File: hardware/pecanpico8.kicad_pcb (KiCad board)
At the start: 4 copper layers, 29.8 x 33.7 mm, 153 parts, among them IC1 SPV1040, IC2 TPS62260, IC3 ADP322ACPZ-115-R7, IC4 Si4464, IC5 STM32F745IGKx, IC6 EVA-7M, IC7 PAC1720, IC8 BME280, P1 CONN_01X25, P2 CONN_01X11, P3 USB_OTG, P4 SMA Edge, P5 CONN_01X02, Q1 FDN306P, X1 KT2016K26000BCW18ZAS

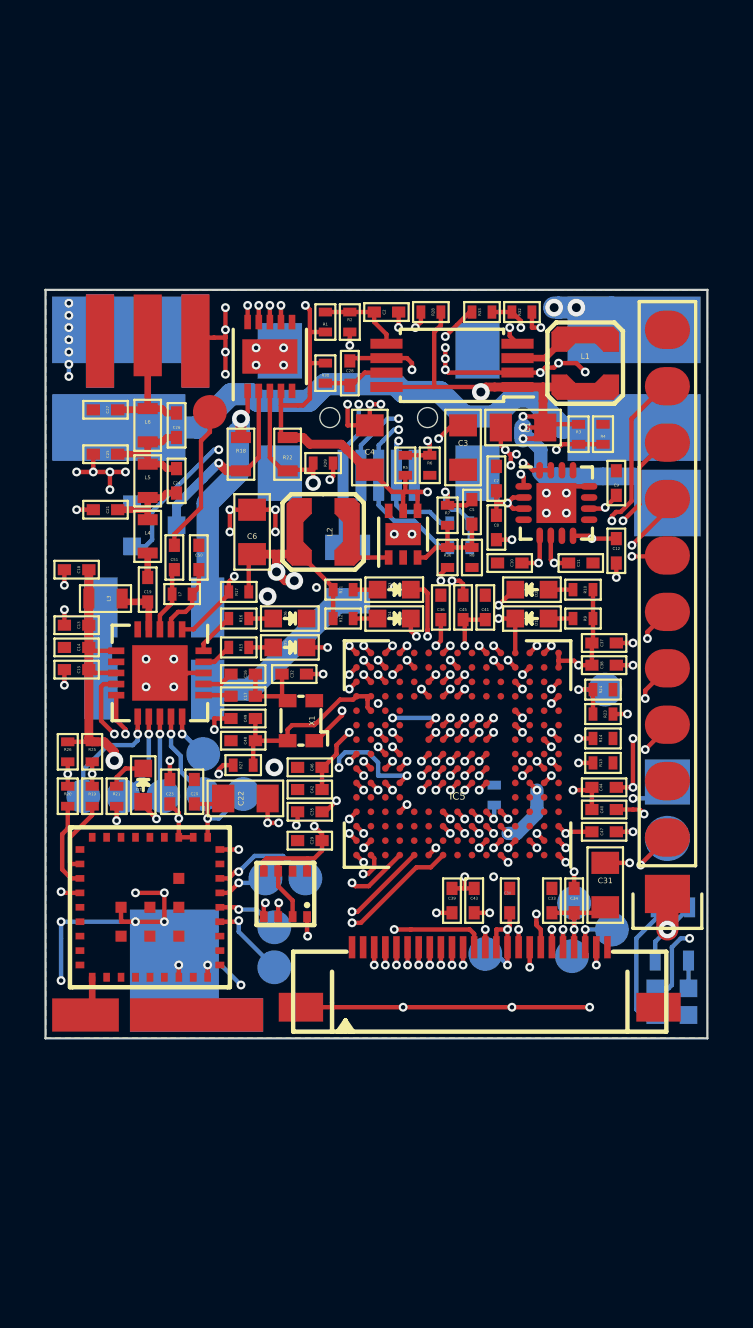
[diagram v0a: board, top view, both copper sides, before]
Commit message: Started developement of rev 8b Changed USB Connector: Mini => Micro Connected CAM_EN to STM32 Added battery jumper switch at programming header Added solar input at programmer header Removed LED outputs at programmer header Removed Testpads at BOOT0 Moved parts around
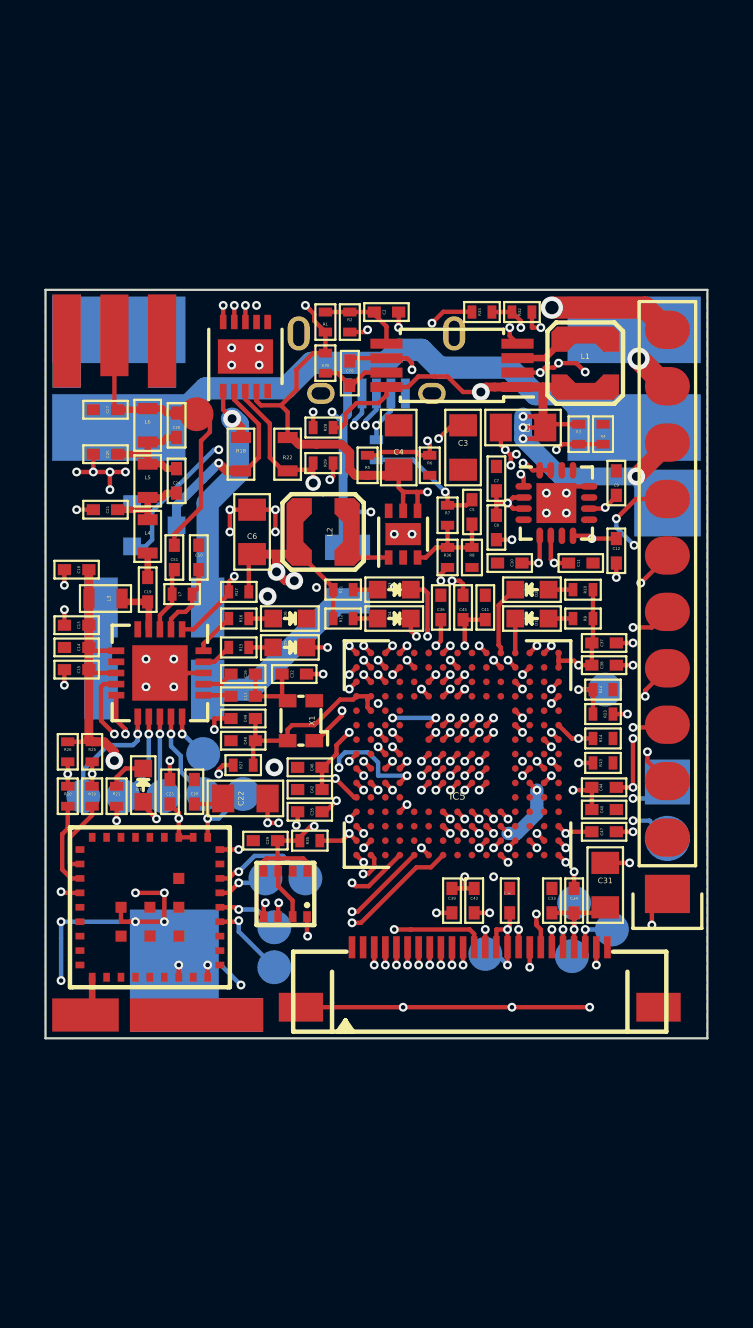
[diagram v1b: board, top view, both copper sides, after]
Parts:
- removed D10: red, stm32f7:LED_0603
- removed D11: yellow, stm32f7:LED_0603
- removed R34: 1k5, stm32f7:R_0603
- removed R37: 330R, stm32f7:R_0603
- removed W1: TEST, stm32f7:R_0402
- P3: footprint Connect:USB_Mini-B -> stm32f7:USB_Micro-B
- R35: moved to F.Cu
- moved R35 14.8 mm to (59.0, 115.7), turned to 0 degrees
- moved R28 7.11 mm to (59.6, 97.1)
- moved R31 5.00 mm to (62.0, 98.1), turned to 90 degrees
- moved C29 2.00 mm to (57.0, 115.7)
- moved P3 1.80 mm to (62.0, 94.0), turned to 0 degrees
- moved R5 1.70 mm to (61.6, 98.8)
- moved P4 1.50 mm to (50.2, 91.1)
- moved C4 1.30 mm to (63.0, 98.0)
- moved IC7 1.10 mm to (56.1, 93.9)
- moved W25 0.61 mm to (53.9, 96.5)
- moved R30 0.45 mm to (59.7, 94.2)
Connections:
- F1 pad 2: Net-(F1-Pad2) -> /USB_VUSB
- IC5 pad E15: Net-(IC5-PadE15) -> /USB_VUSB
- IC5 pad K1: Net-(IC5-PadK1) -> /CAM_EN
- P2 pad 1: +1V8 -> /SWD_SWCLK
- P2 pad 10: /IO_RXD -> /BATT_CONN
- P2 pad 11: GND -> +BATT
- P2 pad 2: /SWD_SWCLK -> GND
- P2 pad 3: GND -> /SWD_SWDIO
- P2 pad 4: /SWD_SWDIO -> /SWD_NRST
- P2 pad 5: /SWD_NRST -> /SWD_SWO
- P2 pad 6: /SWD_SWO -> /IO_TXD
- P2 pad 7: /IO_LED1 -> /IO_RXD
- P2 pad 8: /IO_LED2 -> GND
- P2 pad 9: /IO_TXD -> +SOL
- P3 pad 1: Net-(F1-Pad2) -> /USB_VUSB
- P5 pad 2: GND -> +1V8
- R33 pad 1: Net-(F1-Pad2) -> /USB_VUSB
- W11 pad 1: +BATT -> /BATT_CONN
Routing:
- net /USB_VUSB: track 0.00 -> 32.5 mm, vias 0 -> 4
- net Net-(F1-Pad2): track 13.9 -> 0.00 mm, vias 2 -> 0
- net GND: track 117.5 -> 104.4 mm, vias 131 -> 114
- net /IO_LED1: track 11.8 -> 1.55 mm, vias 2 -> 0
- net /IO_LED2: track 13.4 -> 3.23 mm, vias 3 -> 0
- net /SOL_SHORT_EN: track 37.7 -> 27.7 mm
- net Net-(D11-Pad2): track 5.93 -> 0.00 mm
- net /IO_RXD: track 20.6 -> 15.1 mm
- net /USB_D+: track 29.3 -> 24.3 mm
- net /IO_TXD: track 18.0 -> 13.2 mm
- net +1V8: track 151.7 -> 146.9 mm
- net +SOL: track 50.2 -> 54.1 mm, vias 5 -> 6
- net /SWD_SWO: track 20.0 -> 17.2 mm
- net /USB_ID: track 25.6 -> 22.9 mm
- net /USB_D-: track 27.0 -> 24.4 mm
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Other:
- net class Power: clearance 0.2 -> 0.1
- board text added: "+CORE"
- board text added: "Oct 2016"
- board text added: "Pecan Pico 8b"
- board text removed: "1V8"
- board text removed: "Aug 2016"
- board text removed: "Pecan Pico 8a"

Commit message: GPS
- GPS Antenna went to the backside, so save space.
- We also use IPEX connectors for the GPS Antenna instead but you can also solder a wire on the connector pad instead.

Transmitter

- The space which I won, went into the LPF of the transceiver.
- We use an LFCN LPF by Mini-Circuits. They are more expensive (~US$5) but work perfectly for us.
- We also added a RX/TX switch to it. I did this because an Australian friend found out how to receive AFSK APRS with the Si4464.
- The transmitter also got that fancy IPEX connector for which you can find prebuild 70cm wire-antennas on Ebay for US$1.

Camera

- I discarded the FFC connector and replaced it with a custom 50mil edge-header (on which you can attach a standard 50mil header)
- But we planned to use cameras like these: https://sc02.alicdn.com/kf/HTB1PjEGKVXXXXaYXXXXq6xXFXXX1/2-0-Mega-Pixels-CMOS-OV2640-camera.jpg
- They are soldered on a separate daughter board. That daughter board is directly soldered to the edge of the Pecan. The dautherboard is then looking downwards
- There can be soldered a separated BME280 on the daughterboard too but that's optional

Connectors
- The side connector has a different Pinout. the first 2 pins connect the battery to the circuit itself. By removing a jumper on the header, you may disconnect the battery from the circuit.
- On the bottom you have a BOOT0. That pin got an additional pulldown, so the tracker doesn't fall accidentally into the bootloader.

USB
- I replaced the Mini USB connector with a Micro USB connector while you need much force to remove plug.
- I also connected the USB port to another specific pin on the STM32. While VUSB wasn't connected, USB wouldn't startup unfortunately.
- Connected USB to PB port instead of port PA
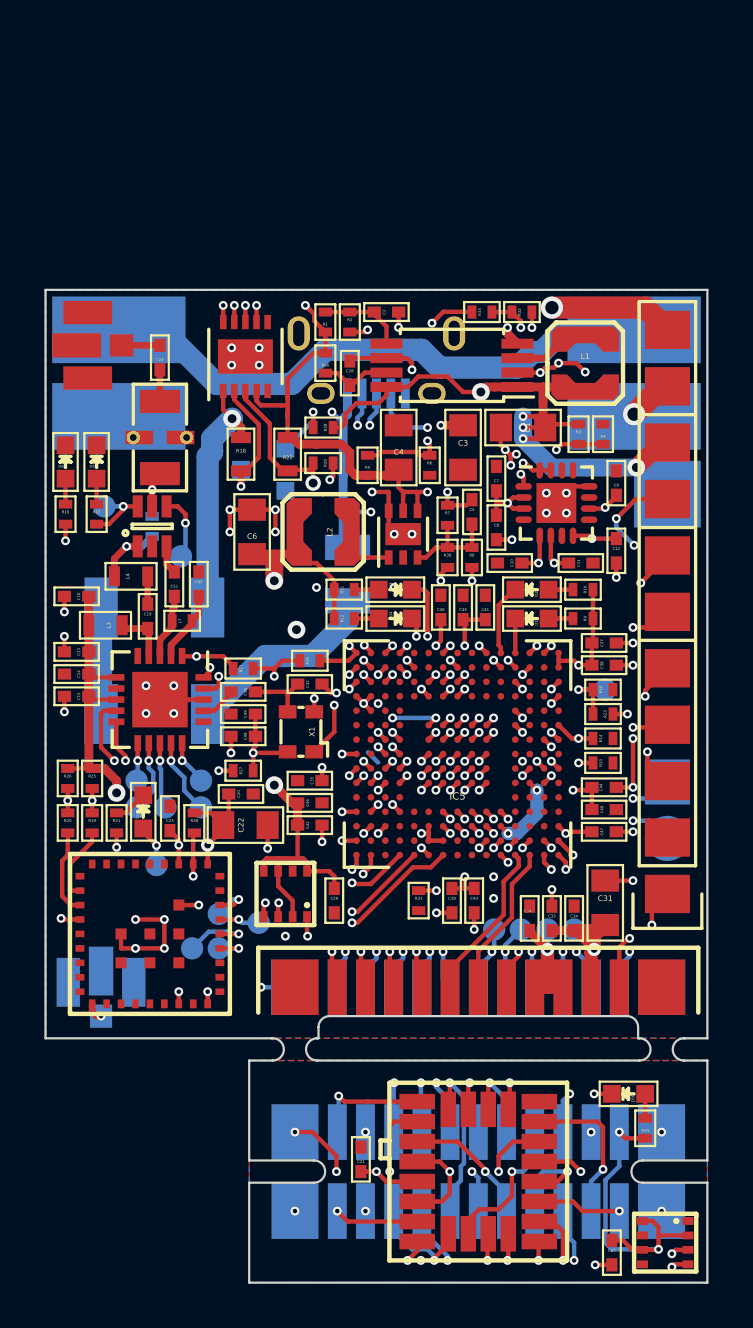
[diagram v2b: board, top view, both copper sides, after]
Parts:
- removed C25, C27: 22p, stm32f7:C_0402
- removed C26: 1p8, stm32f7:C_0402
- removed L5, L6: 68n, stm32f7:R_0603
- removed the REF** at (51.7, 81.0)
- removed W2, W5: Pad, stm32f7:PAD_6x1.5
- removed W25: Pad, Measurement_Points:Measurement_Point_Round-SMD-Pad_Small
- removed W4: Pad, stm32f7:PAD_4x4
- added D10: red, stm32f7:LED_0603, F.Cu at (73.4, 127.1)
- added IC9: BME280, stm32f7:BME280, F.Cu at (75.0, 133.8)
- added P6: IPX 2mm, stm32f7:IPX_2mm, B.Cu at (49.6, 122.1)
- added P7: CONN_02X13, stm32f7:OV2640_Socket, B.Cu at (66.6, 130.6)
- added R34: 0R, stm32f7:R_0402, F.Cu at (74.1, 128.7)
- added R37: 0R, stm32f7:R_0402, B.Cu at (51.9, 101.5)
- added R38: 0R, stm32f7:R_0402, F.Cu at (53.8, 114.9)
- added U1: AS-213, stm32f7:SC-70-6, F.Cu at (51.9, 101.5)
- added U2: LFCN-120, stm32f7:FV1206, F.Cu at (52.2, 97.5)
- added U3: uctronics OV2640, stm32f7:OV2640, F.Cu at (66.6, 130.6)
- added W1: Testpad, stm32f7:Testpad, B.Cu at (49.8, 100.7)
- C17: value NA -> 100n
- C21: value 18p -> 100n
- C24: value 4p7 -> 470p
- P1: value CONN_01X25 -> CONN_02X13; footprint stm32f7:FFC1x24_0.5mm -> stm32f7:OV2640_Header
- P4: value SMA Edge -> IPX 2mm; footprint stm32f7:SMA_EDGE -> stm32f7:IPX_2mm
- R1: value 22k -> 220k
- R2: value 10k -> 100k
- R27: value NA -> 0R
- R31: value NA -> 100k; moved to F.Cu
- W12, W13, W14, W15, W16, W17, W18, W19, W20, W21, W22, W23, W24, W26, W27: footprint Measurement_Points:Measurement_Point_Round-SMD-Pad_Small -> stm32f7:Testpad
- W3: value Pad -> Testpad; footprint stm32f7:PAD_3x1.5 -> stm32f7:Testpad; moved to B.Cu
- moved C21 31.4 mm to (61.3, 130.1), turned to 90 degrees
- moved C17 30.1 mm to (72.6, 134.2), turned to 270 degrees
- moved W3 21.1 mm to (53.2, 102.9)
- moved R31 20.4 mm to (63.9, 118.4), turned to 270 degrees
- moved D6 12.3 mm to (48.0, 98.7), turned to 270 degrees
- moved D5 12.1 mm to (49.4, 98.7), turned to 270 degrees
- moved R16 9.11 mm to (48.0, 101.0), turned to 270 degrees
- moved R15 8.77 mm to (49.4, 101.0), turned to 270 degrees
- moved R35 8.10 mm to (59.0, 107.6)
- moved C24 5.60 mm to (52.2, 94.0)
- moved Q1 5.50 mm to (56.9, 99.0), turned to 270 degrees
- moved W21 5.04 mm to (52.1, 116.8)
- moved REF** 4.40 mm to (44.6, 92.7)
- moved REF** 4.40 mm to (39.6, 92.7)
- moved REF** 4.40 mm to (79.1, 92.7)
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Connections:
- C17 pad 1: /CLOCK_26M -> +1V8
- C17 pad 2: Net-(C17-Pad2) -> GND
- C21 pad 1: Net-(C21-Pad1) -> /OV2640_AVDD
- C24 pad 1: Net-(C21-Pad1) -> Net-(C24-Pad1)
- IC4 pad 16: Net-(C17-Pad2) -> (no net)
- IC4 pad 4: Net-(C19-Pad1) -> Net-(C19-Pad2)
- IC4 pad 7: Net-(IC4-Pad7) -> (no net)
- IC5 pad A13: Net-(IC5-PadA13) -> (no net)
- IC5 pad A2: Net-(IC5-PadA2) -> /CAM_GPIO2
- IC5 pad A3: Net-(IC5-PadA3) -> /CAM_GPIO1
- IC5 pad A4: Net-(IC5-PadA4) -> /CAM_GPIO0
- IC5 pad A6: Net-(IC5-PadA6) -> (no net)
- IC5 pad A7: Net-(IC5-PadA7) -> (no net)
- IC5 pad A8: Net-(IC5-PadA8) -> (no net)
- IC5 pad B10: Net-(IC5-PadB10) -> +IO
- IC5 pad B11: Net-(IC5-PadB11) -> (no net)
- IC5 pad B12: Net-(IC5-PadB12) -> (no net)
- IC5 pad B13: Net-(IC5-PadB13) -> (no net)
- IC5 pad B14: /GPS_IRQ -> (no net)
- IC5 pad B15: /USB_D+ -> /GPS_IRQ
- IC5 pad B7: Net-(IC5-PadB7) -> (no net)
- IC5 pad B8: Net-(IC5-PadB8) -> (no net)
- IC5 pad B9: Net-(IC5-PadB9) -> +IO
- IC5 pad C10: Net-(IC5-PadC10) -> +IO
- IC5 pad C11: Net-(IC5-PadC11) -> (no net)
- IC5 pad C12: Net-(IC5-PadC12) -> (no net)
- IC5 pad C13: Net-(IC5-PadC13) -> /SPI_MOSI
- IC5 pad C14: Net-(IC5-PadC14) -> /SPI_MISO
- IC5 pad C15: /USB_D- -> (no net)
- IC5 pad C2: Net-(IC5-PadC2) -> (no net)
- IC5 pad C3: Net-(IC5-PadC3) -> (no net)
- IC5 pad C4: Net-(IC5-PadC4) -> (no net)
- IC5 pad D1: Net-(IC5-PadD1) -> (no net)
- IC5 pad D10: Net-(IC5-PadD10) -> (no net)
- IC5 pad D11: Net-(IC5-PadD11) -> (no net)
- IC5 pad D13: Net-(IC5-PadD13) -> (no net)
- IC5 pad D14: Net-(IC5-PadD14) -> /SPI_SCK
- IC5 pad D15: /USB_ID -> /RADIO_CS
- IC5 pad D2: Net-(IC5-PadD2) -> (no net)
- IC5 pad D3: Net-(IC5-PadD3) -> (no net)
- IC5 pad D4: Net-(IC5-PadD4) -> (no net)
- IC5 pad E1: Net-(IC5-PadE1) -> (no net)
- IC5 pad E12: Net-(IC5-PadE12) -> (no net)
- IC5 pad E13: Net-(IC5-PadE13) -> (no net)
- IC5 pad E14: Net-(IC5-PadE14) -> (no net)
- IC5 pad E15: /USB_VUSB -> (no net)
- IC5 pad E2: Net-(IC5-PadE2) -> (no net)
- IC5 pad E3: Net-(IC5-PadE3) -> (no net)
- IC5 pad E4: Net-(IC5-PadE4) -> (no net)
- IC5 pad F1: Net-(IC5-PadF1) -> (no net)
- IC5 pad F4: Net-(IC5-PadF4) -> (no net)
- IC5 pad G4: Net-(IC5-PadG4) -> (no net)
- IC5 pad H1: Net-(IC5-PadH1) -> (no net)
- IC5 pad H14: Net-(IC5-PadH14) -> (no net)
- IC5 pad H2: Net-(IC5-PadH2) -> (no net)
- IC5 pad H3: Net-(IC5-PadH3) -> (no net)
- IC5 pad H4: Net-(IC5-PadH4) -> (no net)
- IC5 pad J14: Net-(IC5-PadJ14) -> (no net)
- IC5 pad J15: Net-(IC5-PadJ15) -> (no net)
- IC5 pad J3: Net-(IC5-PadJ3) -> (no net)
- IC5 pad J4: Net-(IC5-PadJ4) -> (no net)
- IC5 pad K12: Net-(IC5-PadK12) -> (no net)
- IC5 pad K13: Net-(IC5-PadK13) -> (no net)
- IC5 pad K14: Net-(IC5-PadK14) -> (no net)
- IC5 pad K15: Net-(IC5-PadK15) -> (no net)
- IC5 pad K2: Net-(IC5-PadK2) -> (no net)
- IC5 pad K3: Net-(IC5-PadK3) -> (no net)
- IC5 pad L1: Net-(IC5-PadL1) -> (no net)
- IC5 pad L12: Net-(IC5-PadL12) -> (no net)
- IC5 pad L13: Net-(IC5-PadL13) -> (no net)
- IC5 pad L15: Net-(IC5-PadL15) -> (no net)
- IC5 pad L2: Net-(IC5-PadL2) -> (no net)
- IC5 pad L3: Net-(IC5-PadL3) -> (no net)
- IC5 pad M11: Net-(IC5-PadM11) -> (no net)
- IC5 pad M12: Net-(IC5-PadM12) -> (no net)
- IC5 pad M13: Net-(IC5-PadM13) -> (no net)
- IC5 pad M2: Net-(IC5-PadM2) -> (no net)
- IC5 pad M3: Net-(IC5-PadM3) -> (no net)
- IC5 pad M4: Net-(IC5-PadM4) -> (no net)
- IC5 pad M5: Net-(IC5-PadM5) -> (no net)
- IC5 pad M6: Net-(IC5-PadM6) -> (no net)
- IC5 pad M7: Net-(IC5-PadM7) -> (no net)
- IC5 pad N11: Net-(IC5-PadN11) -> (no net)
- IC5 pad N12: Net-(IC5-PadN12) -> (no net)
- IC5 pad N13: /RADIO_SDN -> /PAC_ALERT
- IC5 pad N14: /RADIO_IRQ -> /RADIO_GPIO0
- IC5 pad N15: /RADIO_GPIO0 -> /RADIO_IRQ
- IC5 pad N2: Net-(IC5-PadN2) -> (no net)
- IC5 pad N3: Net-(IC5-PadN3) -> (no net)
- IC5 pad N5: Net-(IC5-PadN5) -> (no net)
- IC5 pad N6: Net-(IC5-PadN6) -> (no net)
- IC5 pad N7: Net-(IC5-PadN7) -> (no net)
- IC5 pad P10: Net-(IC5-PadP10) -> (no net)
- IC5 pad P12: /PAC_ALERT -> GND
- IC5 pad P13: /SPI_SCK -> /USB_VUSB
- IC5 pad P14: /RADIO_CS -> /RADIO_SDN
- IC5 pad P2: Net-(IC5-PadP2) -> (no net)
- IC5 pad P6: Net-(IC5-PadP6) -> (no net)
- IC5 pad P7: Net-(IC5-PadP7) -> (no net)
- IC5 pad P9: Net-(IC5-PadP9) -> (no net)
- IC5 pad R10: Net-(IC5-PadR10) -> (no net)
- IC5 pad R11: Net-(IC5-PadR11) -> (no net)
- IC5 pad R14: /SPI_MISO -> /USB_D-
- IC5 pad R15: /SPI_MOSI -> /USB_D+
- IC5 pad R7: Net-(IC5-PadR7) -> (no net)
- IC5 pad R8: Net-(IC5-PadR8) -> (no net)
- IC6 pad 12: Net-(IC6-Pad12) -> (no net)
- IC6 pad 20: +1V8 -> +IO
- IC6 pad 32: Net-(IC6-Pad32) -> (no net)
- IC6 pad 34: Net-(IC6-Pad34) -> (no net)
- IC6 pad 35: Net-(IC6-Pad35) -> (no net)
- IC6 pad 5: Net-(IC6-Pad5) -> (no net)
- IC6 pad 6: Net-(IC6-Pad6) -> (no net)
- IC6 pad 8: Net-(IC6-Pad8) -> (no net)
- L3 pad 1: Net-(C19-Pad1) -> Net-(C19-Pad2)
- L4 pad 1: Net-(C21-Pad1) -> Net-(L4-Pad1)
- L4 pad 2: Net-(C19-Pad2) -> Net-(C19-Pad1)
- P1 pad 1: Net-(P1-Pad1) -> GND
- P1 pad 10: GND -> /CAM_D8
- P1 pad 11: /CAM_D8 -> /CAM_HREF
- P1 pad 12: /CAM_XCLK -> /I2C_SDA
- P1 pad 13: /CAM_D9 -> /CAM_GPIO1
- P1 pad 14: +1V35 -> /I2C_SCL
- P1 pad 15: +1V35 -> /CAM_GPIO0
- P1 pad 16: /CAM_HREF -> /CAM_VSYNC
- P1 pad 17: GND -> /CAM_D7
- P1 pad 18: /CAM_VSYNC -> /CAM_D9
- P1 pad 19: /CAM_RESET -> /CAM_D2
- P1 pad 2: Net-(P1-Pad2) -> GND
- P1 pad 20: /I2C_SCL -> /CAM_PCLK
- P1 pad 21: VDDA -> /CAM_XCLK
- P1 pad 22: /I2C_SDA -> /CAM_D5
- P1 pad 23: GND -> /CAM_D4
- P1 pad 24: Net-(P1-Pad24) -> /CAM_D3
- P1 pad 3: /CAM_D4 -> +1V8
- P1 pad 4: /CAM_D3 -> /CAM_D6
- P1 pad 5: /CAM_D5 -> VDDA
- P1 pad 6: /CAM_D2 -> /CAM_RESET
- P1 pad 7: /CAM_D6 -> +1V35
- P1 pad 8: /CAM_PCLK -> /CAM_GPIO2
- P1 pad 9: /CAM_D7 -> +1V35
- P3 pad 4: /USB_ID -> /V_BOOST
- P4 pad 1: Net-(C26-Pad2) -> Net-(C24-Pad2)
- R31 pad 1: +1V8 -> /BOOT0
- R31 pad 2: /USB_ID -> GND
- W3 pad 1: Net-(IC6-Pad1) -> /RADIO_GPIO3
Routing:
- net /OV2640_D2: track 0.00 -> 23.2 mm, vias 0 -> 3
- net /USB_ID: track 22.9 -> 0.00 mm, vias 2 -> 0
- net /OV2640_SCL: track 0.00 -> 21.4 mm, vias 0 -> 3
- net /RADIO_GPIO3: track 1.92 -> 20.9 mm, vias 0 -> 3
- net /OV2640_D7: track 0.00 -> 18.1 mm, vias 0 -> 2
- net GND: track 104.4 -> 86.8 mm, vias 114 -> 108
- net +1V8: track 146.9 -> 164.4 mm, vias 32 -> 33
- net /RADIO_GPIO2: track 1.40 -> 18.6 mm, vias 0 -> 2
- net /OV2640_SDA: track 0.00 -> 16.8 mm, vias 0 -> 2
- net +IO: track 0.00 -> 16.2 mm, vias 0 -> 2
- net /OV2640_PWDN: track 0.00 -> 15.7 mm, vias 0 -> 2
- net /OV2640_AVDD: track 0.00 -> 15.6 mm, vias 0 -> 2
- net /OV2640_DVDD: track 0.00 -> 14.3 mm, vias 0 -> 2
- net /OV2640_XCLK: track 0.00 -> 12.5 mm, vias 0 -> 2
- net /USB_D-: track 24.4 -> 12.5 mm
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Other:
- board size 29.8 x 33.7 mm -> 29.8 x 44.7 mm
- net class Power: trace_width 1 -> 0.2
- board text added: "+ANALOG"
- board text added: "Jan 2017"
- board text added: "RES"
- board text added: "RXD"
- board text added: "TXD"
- board text added: "VCC"
- board text added: "VCC GPS"
- board text removed: "3V3"
- board text removed: "Oct 2016"
- board text removed: "RESET"
- board text removed: "UART"
- board text removed: "VDDA"
